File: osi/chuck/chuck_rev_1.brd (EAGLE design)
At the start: 25.4 x 25.4 mm, 7 parts

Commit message: chuck
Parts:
- removed I2C_L, I2C_R: (no value), SparkFun_mod:1X05
- removed R1, R2: (no value), adafruit_mod:0204V
- removed RESET: PTS635_SWITCH, _my-parts:PTS635_SWITCH
- added U$1: NUNCHUCKCHUCK, _my-parts:CONN
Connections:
- removed net RESET: RESET.P$2
- net +3V3: now also U$1.VCC; no longer I2C_L.4, I2C_R.2
- net +5V: no longer I2C_L.5, I2C_R.1
- net D1: no longer R2.2
- net D2: no longer R1.2
- net GND: now also U$1.GND; no longer I2C_L.3, I2C_R.3, R1.1, R2.1, RESET.P$1
- net SCL_D4: now also U$1.SCL; no longer I2C_L.1, I2C_R.5
- net SDA_D6: now also U$1.SDA; no longer I2C_L.2, I2C_R.4
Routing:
- net SDA_D6: track 0.00 -> 13.8 mm
- net SCL_D4: track 0.00 -> 9.08 mm
- net +3V3: track 0.00 -> 8.05 mm
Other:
- outline, holes or cut-outs redrawn
- board text added: "CHUCK"
- board text added: "CHUCK Rev 1 Feb 12"
- board text removed: "+5V"
- board text removed: "3V3"
- board text removed: "BRAIN"
- board text removed: "Brain Rev 1 Feb 12"
- board text removed: "RESET"
- board text removed: "SCK"
- board text removed: "SDA"
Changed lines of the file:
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@@
 <wire x1="3.81" y1="25.4" x2="0.000159375" y2="21.590159375" width="0" layer="20"/>
 <wire x1="0.000159375" y1="21.590159375" x2="0" y2="21.590159375" width="0" layer="20"/>
-<wire x1="0" y1="21.590159375" x2="0" y2="0" width="0" layer="20"/>
-<text x="25.146" y="0.381" size="0.8128" layer="21" font="vector" ratio="15" rot="R90">RESET</text>
-<text x="29.21" y="21.336" size="1.27" layer="21" font="vector" ratio="20">BRAIN</text>
-<text x="11.049" y="4.572" size="0.8128" layer="22" font="vector" ratio="15" rot="MR90">MakersBox.blogspot.com</text>
-<text x="13.462" y="4.318" size="1.27" layer="22" font="vector" ratio="15" rot="MR90">One Square Inch</text>
-<text x="37.084" y="18.415" size="1.016" layer="22" font="vector" ratio="12" rot="MR270">Brain
+<wire x1="0" y1="21.590159375" x2="0" y2="19.05" width="0" layer="20"/>
+<wire x1="0" y1="6.35" x2="0" y2="0" width="0" layer="20"/>
+<text x="19.05" y="1.016" size="1.27" layer="21" font="vector" ratio="20">CHUCK</text>
+<text x="14.859" y="4.572" size="0.8128" layer="22" font="vector" ratio="15" rot="MR90">MakersBox.blogspot.com</text>
+<text x="16.002" y="4.318" size="1.27" layer="22" font="vector" ratio="15" rot="MR90">One Square Inch</text>
+<text x="18.415" y="5.334" size="1.016" layer="22" font="vector" ratio="12" rot="MR180">CHUCK
 Rev 1
 Feb 12</text>
-<text x="21.336" y="16.256" size="1.016" layer="21" font="vector" ratio="10">3V3</text>
-<text x="21.336" y="13.589" size="1.016" layer="21" font="vector" ratio="10">GND</text>
-<text x="21.336" y="11.049" size="1.016" layer="21" font="vector" ratio="10">SDA</text>
-<text x="21.336" y="8.509" size="1.016" layer="21" font="vector" ratio="10">SCK</text>
-<text x="20.701" y="17.145" size="1.016" layer="22" font="vector" ratio="15" rot="MR180">3V3</text>
-<text x="20.701" y="14.605" size="1.016" layer="22" font="vector" ratio="15" rot="MR180">GND</text>
-<text x="20.701" y="12.065" size="1.016" layer="22" font="vector" ratio="15" rot="MR180">SDA</text>
-<text x="20.701" y="9.525" size="1.016" layer="22" font="vector" ratio="15" rot="MR180">SCK</text>
-<text x="21.336" y="18.796" size="1.016" layer="21" font="vector" ratio="10">+5V</text>
-<text x="20.955" y="19.685" size="1.016" layer="22" font="vector" ratio="15" rot="MR180">5V</text>
 <text x="1.905" y="2.794" size="1.016" layer="22" font="vector" ratio="15" rot="MR0">V+</text>
 <text x="5.08" y="2.794" size="1.016" layer="22" font="vector" ratio="15" rot="MR0">GND</text>
@@
 </autorouter>
 <elements>
-<element name="RESET" library="_my-parts" package="PTS635_SWITCH" value="PTS635_SWITCH" x="16.51" y="1.905"/>
-<element name="I2C_L" library="SparkFun_mod" package="1X05" value="" x="19.685" y="7.62" rot="R90"/>
-<element name="I2C_R" library="SparkFun_mod" package="1X05" value="" x="5.715" y="17.78" rot="R270"/>
 <element name="JP6" library="SparkFun" package="1X06" value="" x="1.27" y="1.27"/>
 <element name="JP8" library="SparkFun" package="1X08" value="" x="6.35" y="24.13"/>
-<element name="R1" library="adafruit_mod" package="0204V" value="" x="1.27" y="-5.08"/>
-<element name="R2" library="adafruit_mod" package="0204V" value="" x="1.27" y="-10.16"/>
+<element name="U$1" library="_my-parts" package="CONN" value="NUNCHUCKCHUCK" x="10.16" y="7.62"/>
 </elements>
 <signals>
@@
 <vertex x="-0.635" y="-0.635"/>
 </polygon>
-<contactref element="RESET" pad="P$1"/>
-<contactref element="I2C_L" pad="3"/>
-<contactref element="I2C_R" pad="3"/>
 <contactref element="JP6" pad="2"/>
-<contactref element="R1" pad="1"/>
-<contactref element="R2" pad="1"/>
-<wire x1="16.51" y1="1.905" x2="19.685" y2="12.7" width="0" layer="19" extent="1-1"/>
-<wire x1="3.81" y1="1.27" x2="16.51" y2="1.905" width="0" layer="19" extent="1-1"/>
-<wire x1="0" y1="-5.08" x2="3.81" y2="1.27" width="0" layer="19" extent="1-1"/>
-<wire x1="0" y1="-10.16" x2="0" y2="-5.08" width="0" layer="19" extent="1-1"/>
-<wire x1="5.715" y1="12.7" x2="3.81" y2="1.27" width="0" layer="19" extent="1-1"/>
-</signal>
-<signal name="RESET">
-<contactref element="RESET" pad="P$2"/>
+<contactref element="U$1" pad="GND"/>
 </signal>
 <signal name="SDA_D6">
-<contactref element="I2C_L" pad="2"/>
-<contactref element="I2C_R" pad="4"/>
 <contactref element="JP8" pad="2"/>
-<wire x1="5.715" y1="10.16" x2="19.685" y2="10.16" width="0" layer="19" extent="1-1"/>
-<wire x1="8.89" y1="24.13" x2="5.715" y2="10.16" width="0" layer="19" extent="1-1"/>
+<contactref element="U$1" pad="SDA"/>
+<wire x1="8.89" y1="24.13" x2="8.89" y2="22.86" width="0.4064" layer="16"/>
+<wire x1="8.89" y1="22.86" x2="12.7" y2="19.05" width="0.4064" layer="16"/>
+<wire x1="12.7" y1="19.05" x2="12.7" y2="15.24" width="0.4064" layer="16"/>
+<wire x1="12.7" y1="15.24" x2="11.43" y2="13.97" width="0.4064" layer="16"/>
+<wire x1="11.43" y1="13.97" x2="9.93" y2="13.97" width="0.4064" layer="16"/>
 </signal>
 <signal name="SCL_D4">
-<contactref element="I2C_L" pad="1"/>
-<contactref element="I2C_R" pad="5"/>
 <contactref element="JP8" pad="4"/>
-<wire x1="5.715" y1="7.62" x2="19.685" y2="7.62" width="0" layer="19" extent="1-1"/>
-<wire x1="13.97" y1="24.13" x2="5.715" y2="7.62" width="0" layer="19" extent="1-1"/>
+<contactref element="U$1" pad="SCL"/>
+<wire x1="13.97" y1="24.13" x2="13.97" y2="20.042" width="0.4064" layer="1"/>
+<wire x1="13.97" y1="20.042" x2="10.438" y2="16.51" width="0.4064" layer="1"/>
 </signal>
 <signal name="+3V3">
-<contactref element="I2C_L" pad="4"/>
-<contactref element="I2C_R" pad="2"/>
 <contactref element="JP6" pad="4"/>
-<wire x1="5.715" y1="15.24" x2="19.685" y2="15.24" width="0" layer="19" extent="1-1"/>
-<wire x1="8.89" y1="1.27" x2="5.715" y2="15.24" width="0" layer="19" extent="1-1"/>
+<contactref element="U$1" pad="VCC"/>
+<wire x1="9.93" y1="8.89" x2="9.93" y2="2.31" width="0.4064" layer="1"/>
+<wire x1="9.93" y1="2.31" x2="8.89" y2="1.27" width="0.4064" layer="1"/>
 </signal>
 <signal name="+5V">
-<contactref element="I2C_L" pad="5"/>
-<contactref element="I2C_R" pad="1"/>
 <contactref element="JP6" pad="3"/>
-<wire x1="5.715" y1="17.78" x2="19.685" y2="17.78" width="0" layer="19" extent="1-1"/>
-<wire x1="6.35" y1="1.27" x2="5.715" y2="17.78" width="0" layer="19" extent="1-1"/>
 </signal>
 <signal name="D9">
@@
 <signal name="D2">
 <contactref element="JP8" pad="6"/>
-<contactref element="R1" pad="2"/>
-<wire x1="2.54" y1="-5.08" x2="19.05" y2="24.13" width="0" layer="19" extent="1-1"/>
 </signal>
 <signal name="D1">
 <contactref element="JP8" pad="7"/>
-<contactref element="R2" pad="2"/>
-<wire x1="2.54" y1="-10.16" x2="21.59" y2="24.13" width="0" layer="19" extent="1-1"/>
 </signal>
 <signal name="AREF_D0">

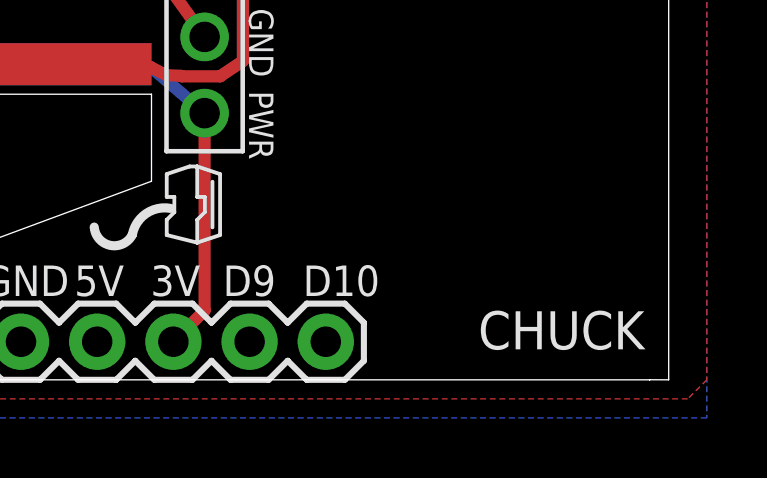
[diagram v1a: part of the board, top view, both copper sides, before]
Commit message: D9 -> D8 for INT0
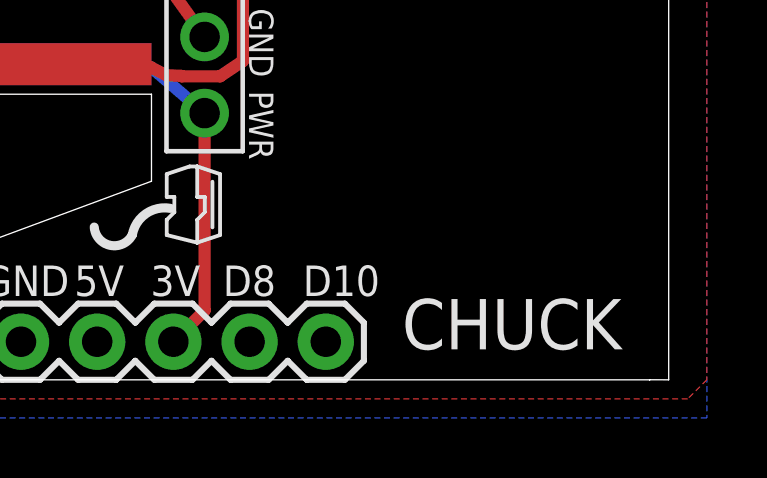
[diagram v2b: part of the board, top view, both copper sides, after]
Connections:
- net D9 renamed D8
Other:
- board text added: "D8"
- board text removed: "D9"
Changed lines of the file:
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@@
 <wire x1="0" y1="21.590159375" x2="0" y2="19.05" width="0" layer="20"/>
 <wire x1="0" y1="6.35" x2="0" y2="0" width="0" layer="20"/>
-<text x="19.05" y="1.016" size="1.27" layer="21" font="vector" ratio="20">CHUCK</text>
+<text x="16.51" y="1.016" size="1.6764" layer="21" font="vector" ratio="20">CHUCK</text>
 <text x="14.859" y="4.572" size="0.8128" layer="22" font="vector" ratio="15" rot="MR90">MakersBox.blogspot.com</text>
 <text x="16.002" y="4.318" size="1.27" layer="22" font="vector" ratio="15" rot="MR90">One Square Inch</text>
@@
 <text x="7.239" y="2.794" size="1.016" layer="22" font="vector" ratio="15" rot="MR0">5V</text>
 <text x="9.652" y="2.794" size="1.016" layer="22" font="vector" ratio="15" rot="MR0">3V</text>
-<text x="12.065" y="2.794" size="1.016" layer="22" font="vector" ratio="15" rot="MR0">D9</text>
+<text x="12.065" y="2.794" size="1.016" layer="22" font="vector" ratio="15" rot="MR0">D8</text>
 <text x="15.367" y="2.794" size="1.016" layer="22" font="vector" ratio="15" rot="MR0">D10</text>
 <text x="24.892" y="21.844" size="1.016" layer="22" font="vector" ratio="15" rot="MR0">D0</text>
@@
 <text x="5.588" y="2.794" size="1.016" layer="21" font="vector" ratio="15">5V</text>
 <text x="8.128" y="2.794" size="1.016" layer="21" font="vector" ratio="15">3V</text>
-<text x="10.541" y="2.794" size="1.016" layer="21" font="vector" ratio="15">D9</text>
+<text x="10.541" y="2.794" size="1.016" layer="21" font="vector" ratio="15">D8</text>
 <text x="13.208" y="2.794" size="1.016" layer="21" font="vector" ratio="15">D10</text>
 </plain>
@@
 <contactref element="JP6" pad="3"/>
 </signal>
-<signal name="D9">
+<signal name="D8">
 <contactref element="JP6" pad="5"/>
 </signal>
